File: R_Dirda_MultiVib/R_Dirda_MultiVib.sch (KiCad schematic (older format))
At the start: 11 parts

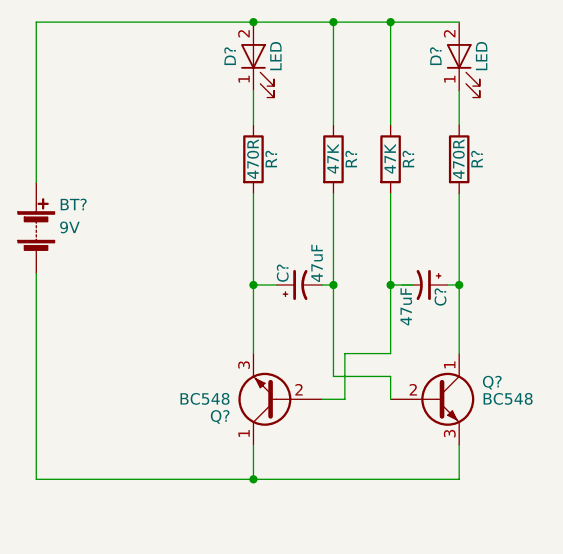
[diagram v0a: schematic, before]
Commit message: Tranzistori aizstati ar IC mikroshemu
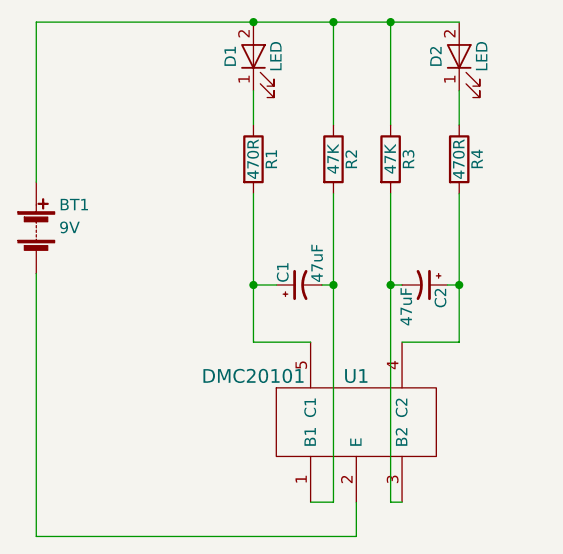
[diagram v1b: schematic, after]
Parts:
- removed Q? (x2): BC548, TO_SOT_Packages_THT:TO-92_Molded_Narrow, symbol BC548
- added U1: DMC20101, symbol DMC20101
- gave numbers to parts that had none: 9
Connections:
- wire segments 23 -> 21
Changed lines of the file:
@@
 LIBS:contrib
 LIBS:valves
-LIBS:2018-cache
+LIBS:bcm586ds
+LIBS:dmc20101
+LIBS:R_Dirda_MultiVib-cache
 EELAYER 25 0
 EELAYER END
@@
 $EndDescr
 $Comp
-L LED D?
+L LED D1
 U 1 1 5A8E904A
 P 2650 2750
-F 0 "D?" H 2650 2850 50  0000 C CNN
+F 0 "D1" H 2650 2850 50  0000 C CNN
 F 1 "LED" H 2650 2650 50  0000 C CNN
 F 2 "" H 2650 2750 50  0001 C CNN
@@
 $EndComp
 $Comp
-L LED D?
+L LED D2
 U 1 1 5A8E90A6
 P 3550 2750
-F 0 "D?" H 3550 2850 50  0000 C CNN
+F 0 "D2" H 3550 2850 50  0000 C CNN
 F 1 "LED" H 3550 2650 50  0000 C CNN
 F 2 "" H 3550 2750 50  0001 C CNN
@@
 $EndComp
 $Comp
-L R R?
+L R R1
 U 1 1 5A8E915E
 P 2650 3200
-F 0 "R?" V 2730 3200 50  0000 C CNN
+F 0 "R1" V 2730 3200 50  0000 C CNN
 F 1 "470R" V 2650 3200 50  0000 C CNN
 F 2 "" V 2580 3200 50  0001 C CNN
@@
 $EndComp
 $Comp
-L R R?
+L R R2
 U 1 1 5A8E91B0
 P 3000 3200
-F 0 "R?" V 3080 3200 50  0000 C CNN
+F 0 "R2" V 3080 3200 50  0000 C CNN
 F 1 "47K" V 3000 3200 50  0000 C CNN
 F 2 "" V 2930 3200 50  0001 C CNN
@@
 $EndComp
 $Comp
-L R R?
+L R R3
 U 1 1 5A8E91F7
 P 3250 3200
-F 0 "R?" V 3330 3200 50  0000 C CNN
+F 0 "R3" V 3330 3200 50  0000 C CNN
 F 1 "47K" V 3250 3200 50  0000 C CNN
 F 2 "" V 3180 3200 50  0001 C CNN
@@
 $EndComp
 $Comp
-L R R?
+L R R4
 U 1 1 5A8E922C
 P 3550 3200
-F 0 "R?" V 3630 3200 50  0000 C CNN
+F 0 "R4" V 3630 3200 50  0000 C CNN
 F 1 "470R" V 3550 3200 50  0000 C CNN
 F 2 "" V 3480 3200 50  0001 C CNN
@@
 $EndComp
 $Comp
-L Battery BT?
+L Battery BT1
 U 1 1 5A8E9273
 P 1700 3500
-F 0 "BT?" H 1800 3600 50  0000 L CNN
+F 0 "BT1" H 1800 3600 50  0000 L CNN
 F 1 "9V" H 1800 3500 50  0000 L CNN
 F 2 "" V 1700 3560 50  0001 C CNN
@@
 $EndComp
 $Comp
-L CP1_Small C?
+L CP1_Small C1
 U 1 1 5A8E92BC
 P 2850 3750
-F 0 "C?" H 2860 3820 50  0000 L CNN
+F 0 "C1" H 2860 3820 50  0000 L CNN
 F 1 "47uF" H 2860 3670 50  0000 L CNN
 F 2 "" H 2850 3750 50  0001 C CNN
@@
 $EndComp
 $Comp
-L CP1_Small C?
+L CP1_Small C2
 U 1 1 5A8E9336
 P 3400 3750
-F 0 "C?" H 3410 3820 50  0000 L CNN
+F 0 "C2" H 3410 3820 50  0000 L CNN
 F 1 "47uF" H 3410 3670 50  0000 L CNN
 F 2 "" H 3400 3750 50  0001 C CNN
@@
 	0    1    1    0
 $EndComp
-$Comp
-L BC548 Q?
-U 1 1 5A8E938D
-P 2750 4250
-F 0 "Q?" H 2950 4325 50  0000 L CNN
-F 1 "BC548" H 2950 4250 50  0000 L CNN
-F 2 "TO_SOT_Packages_THT:TO-92_Molded_Narrow" H 2950 4175 50  0001 L CIN
-F 3 "" H 2750 4250 50  0001 L CNN
-	1    2750 4250
-	-1   0    0    1
-$EndComp
-$Comp
-L BC548 Q?
-U 1 1 5A8E940A
-P 3450 4250
-F 0 "Q?" H 3650 4325 50  0000 L CNN
-F 1 "BC548" H 3650 4250 50  0000 L CNN
-F 2 "TO_SOT_Packages_THT:TO-92_Molded_Narrow" H 3650 4175 50  0001 L CIN
-F 3 "" H 3450 4250 50  0001 L CNN
-	1    3450 4250
-	1    0    0    -1
-$EndComp
 Wire Wire Line
 	2650 2900 2650 3050
-Wire Wire Line
-	2650 3350 2650 4050
 Wire Wire Line
 	2750 3750 2650 3750
@@
 	2950 3750 3000 3750
 Wire Wire Line
-	3000 3350 3000 4150
+	3000 3350 3000 4700
 Wire Wire Line
 	1700 2600 1700 3300
 Connection ~ 2650 2600
 Wire Wire Line
-	1700 3700 1700 4600
-Wire Wire Line
-	2650 4600 2650 4450
+	1700 3700 1700 4850
 Wire Wire Line
 	3250 3050 3250 2600
 Connection ~ 3250 2600
 Wire Wire Line
-	3250 3350 3250 4050
-Wire Wire Line
-	3250 3750 3350 3750
-Wire Wire Line
-	3550 3350 3550 4050
+	3250 3350 3250 4700
 Wire Wire Line
 	3550 3750 3500 3750
-Wire Wire Line
-	3250 4050 3050 4050
-Wire Wire Line
-	3050 4050 3050 4250
-Wire Wire Line
-	3050 4250 2950 4250
 Connection ~ 3250 3750
 Connection ~ 3000 3750
-Connection ~ 2650 4600
+Connection ~ 3550 3750
+$Comp
+L DMC20101 U1
+U 1 1 5AA92E73
+P 3100 4350
+F 0 "U1" H 3100 4550 60  0000 C CNN
+F 1 "DMC20101" H 2650 4550 60  0000 C CNN
+F 2 "" H 2650 4550 60  0001 C CNN
+F 3 "" H 2650 4550 60  0001 C CNN
+	1    3100 4350
+	1    0    0    -1
+$EndComp
 Wire Wire Line
-	3550 4600 3550 4450
-Connection ~ 3550 3750
+	2650 3350 2650 4000
 Wire Wire Line
-	3250 4150 3250 4250
+	3550 3350 3550 4000
 Wire Wire Line
-	3000 4150 3250 4150
+	3550 4000 3300 4000
 Wire Wire Line
-	1700 4600 3550 4600
+	2650 4000 2900 4000
+Wire Wire Line
+	3100 4700 3100 4850
+Wire Wire Line
+	3100 4850 1700 4850
+Wire Wire Line
+	3000 4700 2900 4700
+Wire Wire Line
+	3250 4700 3300 4700
+Wire Wire Line
+	3300 3750 3250 3750
 $EndSCHEMATC

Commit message: 0.2
Tranzistori BC548 tiek aizstati ar IC mikroshemu

This reverts commit 3d703b0aae8bc0295c59cc91b30c956ba27862da.
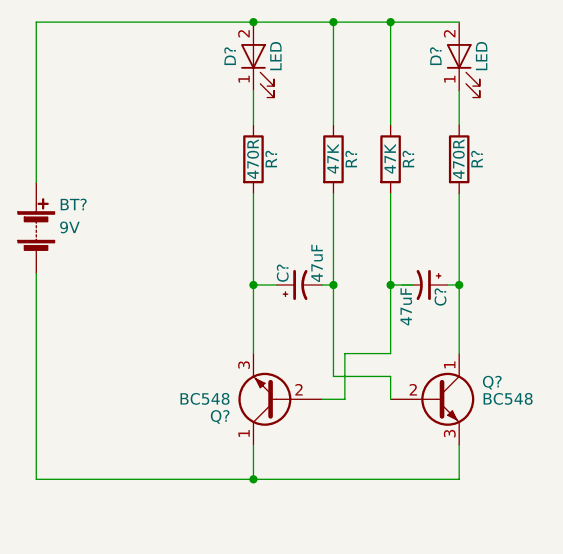
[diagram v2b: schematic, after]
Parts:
- removed U1: DMC20101, symbol DMC20101
- added Q? (x2): BC548, TO_SOT_Packages_THT:TO-92_Molded_Narrow, symbol BC548
- renumbered BT1 to BT?, C1 to C?, C2 to C?, D1 to D?, D2 to D?, R1 to R?, R2 to R?, R3 to R?, R4 to R?
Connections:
- wire segments 21 -> 23
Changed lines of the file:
@@
 LIBS:contrib
 LIBS:valves
-LIBS:bcm586ds
-LIBS:dmc20101
-LIBS:R_Dirda_MultiVib-cache
+LIBS:2018-cache
 EELAYER 25 0
 EELAYER END
@@
 $EndDescr
 $Comp
-L LED D1
+L LED D?
 U 1 1 5A8E904A
 P 2650 2750
-F 0 "D1" H 2650 2850 50  0000 C CNN
+F 0 "D?" H 2650 2850 50  0000 C CNN
 F 1 "LED" H 2650 2650 50  0000 C CNN
 F 2 "" H 2650 2750 50  0001 C CNN
@@
 $EndComp
 $Comp
-L LED D2
+L LED D?
 U 1 1 5A8E90A6
 P 3550 2750
-F 0 "D2" H 3550 2850 50  0000 C CNN
+F 0 "D?" H 3550 2850 50  0000 C CNN
 F 1 "LED" H 3550 2650 50  0000 C CNN
 F 2 "" H 3550 2750 50  0001 C CNN
@@
 $EndComp
 $Comp
-L R R1
+L R R?
 U 1 1 5A8E915E
 P 2650 3200
-F 0 "R1" V 2730 3200 50  0000 C CNN
+F 0 "R?" V 2730 3200 50  0000 C CNN
 F 1 "470R" V 2650 3200 50  0000 C CNN
 F 2 "" V 2580 3200 50  0001 C CNN
@@
 $EndComp
 $Comp
-L R R2
+L R R?
 U 1 1 5A8E91B0
 P 3000 3200
-F 0 "R2" V 3080 3200 50  0000 C CNN
+F 0 "R?" V 3080 3200 50  0000 C CNN
 F 1 "47K" V 3000 3200 50  0000 C CNN
 F 2 "" V 2930 3200 50  0001 C CNN
@@
 $EndComp
 $Comp
-L R R3
+L R R?
 U 1 1 5A8E91F7
 P 3250 3200
-F 0 "R3" V 3330 3200 50  0000 C CNN
+F 0 "R?" V 3330 3200 50  0000 C CNN
 F 1 "47K" V 3250 3200 50  0000 C CNN
 F 2 "" V 3180 3200 50  0001 C CNN
@@
 $EndComp
 $Comp
-L R R4
+L R R?
 U 1 1 5A8E922C
 P 3550 3200
-F 0 "R4" V 3630 3200 50  0000 C CNN
+F 0 "R?" V 3630 3200 50  0000 C CNN
 F 1 "470R" V 3550 3200 50  0000 C CNN
 F 2 "" V 3480 3200 50  0001 C CNN
@@
 $EndComp
 $Comp
-L Battery BT1
+L Battery BT?
 U 1 1 5A8E9273
 P 1700 3500
-F 0 "BT1" H 1800 3600 50  0000 L CNN
+F 0 "BT?" H 1800 3600 50  0000 L CNN
 F 1 "9V" H 1800 3500 50  0000 L CNN
 F 2 "" V 1700 3560 50  0001 C CNN
@@
 $EndComp
 $Comp
-L CP1_Small C1
+L CP1_Small C?
 U 1 1 5A8E92BC
 P 2850 3750
-F 0 "C1" H 2860 3820 50  0000 L CNN
+F 0 "C?" H 2860 3820 50  0000 L CNN
 F 1 "47uF" H 2860 3670 50  0000 L CNN
 F 2 "" H 2850 3750 50  0001 C CNN
@@
 $EndComp
 $Comp
-L CP1_Small C2
+L CP1_Small C?
 U 1 1 5A8E9336
 P 3400 3750
-F 0 "C2" H 3410 3820 50  0000 L CNN
+F 0 "C?" H 3410 3820 50  0000 L CNN
 F 1 "47uF" H 3410 3670 50  0000 L CNN
 F 2 "" H 3400 3750 50  0001 C CNN
@@
 	0    1    1    0
 $EndComp
+$Comp
+L BC548 Q?
+U 1 1 5A8E938D
+P 2750 4250
+F 0 "Q?" H 2950 4325 50  0000 L CNN
+F 1 "BC548" H 2950 4250 50  0000 L CNN
+F 2 "TO_SOT_Packages_THT:TO-92_Molded_Narrow" H 2950 4175 50  0001 L CIN
+F 3 "" H 2750 4250 50  0001 L CNN
+	1    2750 4250
+	-1   0    0    1
+$EndComp
+$Comp
+L BC548 Q?
+U 1 1 5A8E940A
+P 3450 4250
+F 0 "Q?" H 3650 4325 50  0000 L CNN
+F 1 "BC548" H 3650 4250 50  0000 L CNN
+F 2 "TO_SOT_Packages_THT:TO-92_Molded_Narrow" H 3650 4175 50  0001 L CIN
+F 3 "" H 3450 4250 50  0001 L CNN
+	1    3450 4250
+	1    0    0    -1
+$EndComp
 Wire Wire Line
 	2650 2900 2650 3050
+Wire Wire Line
+	2650 3350 2650 4050
 Wire Wire Line
 	2750 3750 2650 3750
@@
 	2950 3750 3000 3750
 Wire Wire Line
-	3000 3350 3000 4700
+	3000 3350 3000 4150
 Wire Wire Line
 	1700 2600 1700 3300
 Connection ~ 2650 2600
 Wire Wire Line
-	1700 3700 1700 4850
+	1700 3700 1700 4600
+Wire Wire Line
+	2650 4600 2650 4450
 Wire Wire Line
 	3250 3050 3250 2600
 Connection ~ 3250 2600
 Wire Wire Line
-	3250 3350 3250 4700
+	3250 3350 3250 4050
+Wire Wire Line
+	3250 3750 3350 3750
+Wire Wire Line
+	3550 3350 3550 4050
 Wire Wire Line
 	3550 3750 3500 3750
+Wire Wire Line
+	3250 4050 3050 4050
+Wire Wire Line
+	3050 4050 3050 4250
+Wire Wire Line
+	3050 4250 2950 4250
 Connection ~ 3250 3750
 Connection ~ 3000 3750
+Connection ~ 2650 4600
+Wire Wire Line
+	3550 4600 3550 4450
 Connection ~ 3550 3750
-$Comp
-L DMC20101 U1
-U 1 1 5AA92E73
-P 3100 4350
-F 0 "U1" H 3100 4550 60  0000 C CNN
-F 1 "DMC20101" H 2650 4550 60  0000 C CNN
-F 2 "" H 2650 4550 60  0001 C CNN
-F 3 "" H 2650 4550 60  0001 C CNN
-	1    3100 4350
-	1    0    0    -1
-$EndComp
 Wire Wire Line
-	2650 3350 2650 4000
+	3250 4150 3250 4250
 Wire Wire Line
-	3550 3350 3550 4000
+	3000 4150 3250 4150
 Wire Wire Line
-	3550 4000 3300 4000
-Wire Wire Line
-	2650 4000 2900 4000
-Wire Wire Line
-	3100 4700 3100 4850
-Wire Wire Line
-	3100 4850 1700 4850
-Wire Wire Line
-	3000 4700 2900 4700
-Wire Wire Line
-	3250 4700 3300 4700
-Wire Wire Line
-	3300 3750 3250 3750
+	1700 4600 3550 4600
 $EndSCHEMATC
